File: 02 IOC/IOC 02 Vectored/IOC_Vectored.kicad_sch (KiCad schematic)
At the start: 6 parts, among them J1 ICSP, SW1 SW_DIP_x08, U1 PIC18F47Q43-I/PT

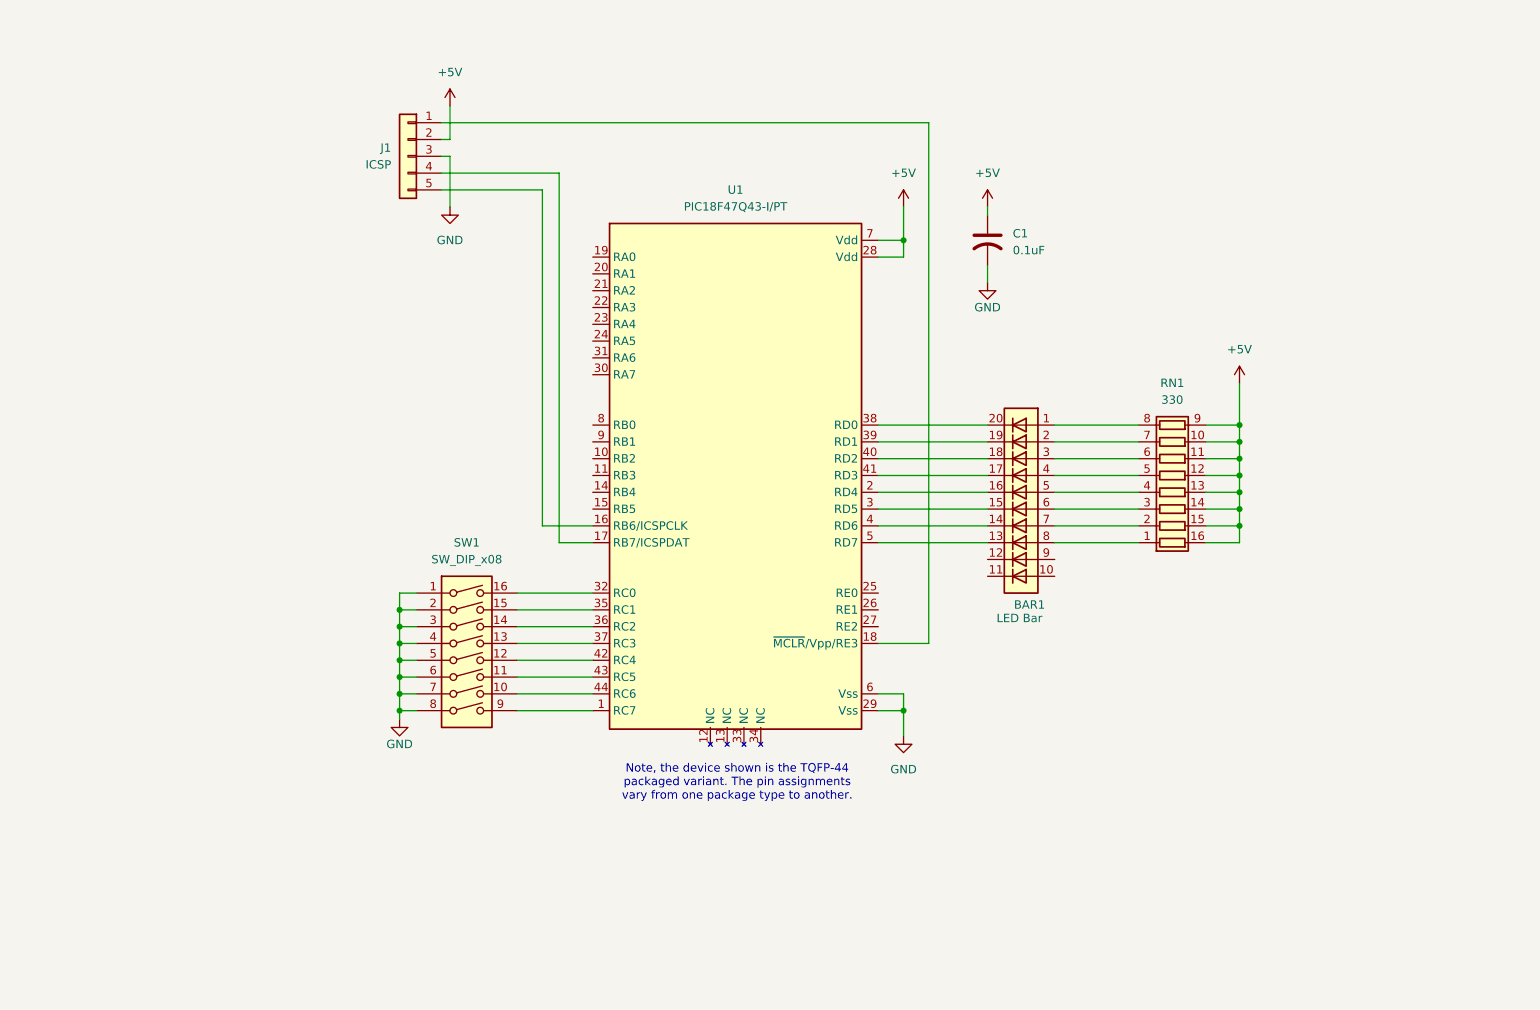
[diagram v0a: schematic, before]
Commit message: Update documentation and schematics for UART and IOC projects
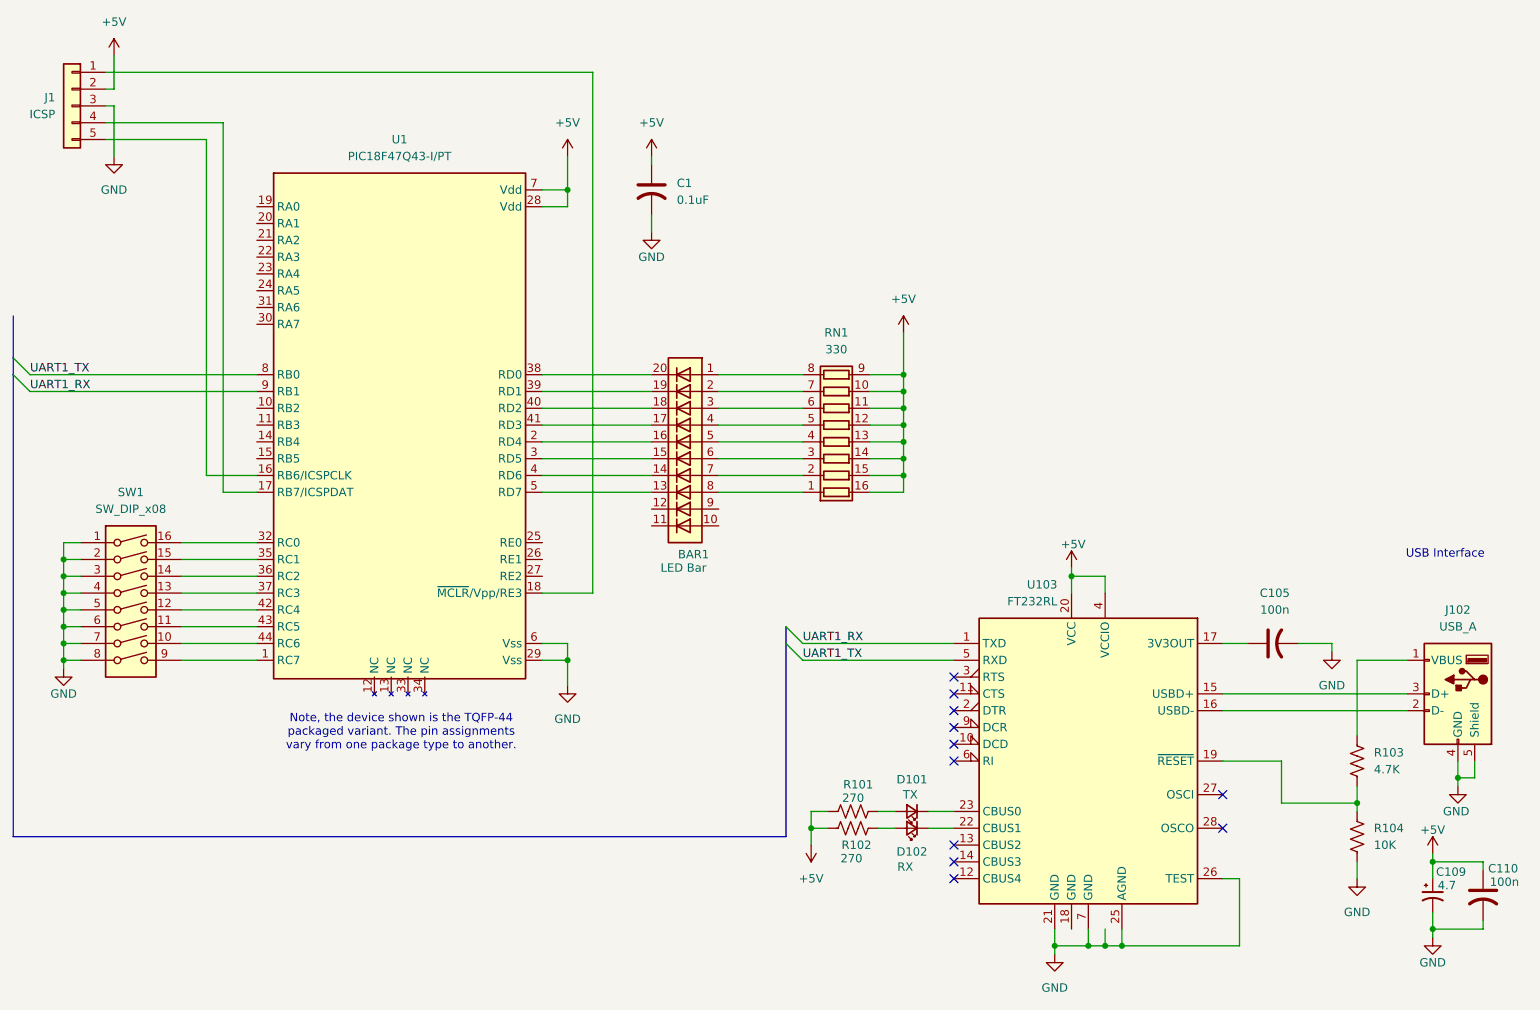
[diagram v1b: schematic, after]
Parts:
- added C105, C110: 100n, symbol Device:C_US
- added C109: 4.7, symbol Device:C_Polarized_Small_US
- added D101: TX, symbol Device:LED_Small
- added D102: RX, symbol Device:LED_Small
- added J102: USB_A, symbol Connector:USB_A
- added R101, R102: 270, symbol Device:R_US
- added R103: 4.7K, symbol Device:R_US
- added R104: 10K, symbol Device:R_US
- added U103: FT232RL, Package_SO:SSOP-28_5.3x10.2mm_P0.65mm, symbol Interface_USB:FT232RL
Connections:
- net +5V: now also C109.1, C110.1, R101.1, R102.1, U103.20 (VCC), U103.4 (VCCIO)
- net GND: now also C105.2, C109.2, C110.2, J102.4 (GND), J102.5 (Shield), R104.2, U103.21 (GND), U103.25 (AGND), U103.26 (TEST), U103.7 (GND)
- net UART1_TX: now reaches U1.8 (RB0)
- net UART1_TX: now also U103.5 (RXD)
- net UART1_RX: now reaches U1.9 (RB1)
- net UART1_RX: now also U103.1 (TXD)
- new net: D102.1 (K), U103.22 (CBUS1)
- new net: D102.2 (A), R102.2
- new net: J102.1 (VBUS), R103.1
- new net: R103.2, R104.1, U103.19 (~{RESET})
- new net: D101.1 (K), U103.23 (CBUS0)
- new net: D101.2 (A), R101.2
- new net: J102.2 (D-), U103.16 (USBD-)
- new net: J102.3 (D+), U103.15 (USBD+)
- new net: C105.1, U103.17 (3V3OUT)
- no-connect marks 0 -> 11
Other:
- note added: "USB Interface"
- moved on the sheet: BAR1, C1, J1, RN1, SW1, U1
